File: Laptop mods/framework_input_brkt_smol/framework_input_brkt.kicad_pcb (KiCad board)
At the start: 2 copper layers, 18 x 7.8 mm, 7 parts, among them J1 FPR_LED, J2 input_conn, J3 PWRSW, J4 USB, J6 KBL

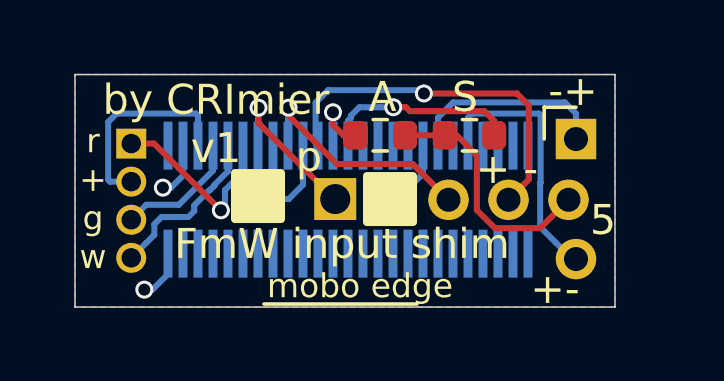
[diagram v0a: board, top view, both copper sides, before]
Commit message: framework_input_brkt_smol: adding resistor to RGW LED, adding Amphenol connector STEP, changing on-board PCB name
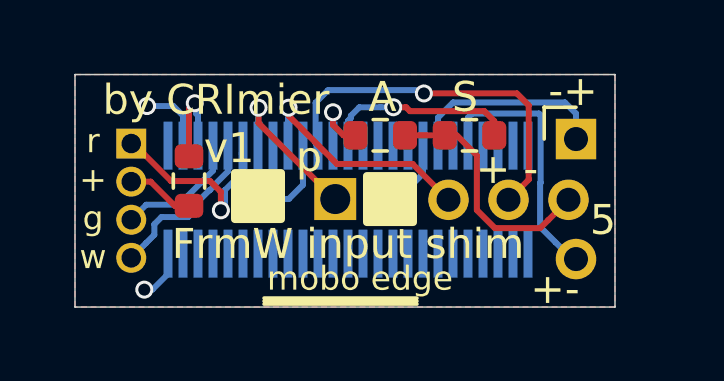
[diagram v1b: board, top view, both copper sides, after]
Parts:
- added R3: 560R, Resistor_SMD:R_0603_1608Metric, F.Cu at (147.8, 99.8)
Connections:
- J1 pad 2: /FPR_LED_COM_5V -> Net-(J1-Pad2)
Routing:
- net /FPR_LED_COM_5V: track 6.86 -> 3.19 mm, vias 0 -> 1
- net Net-(J1-Pad2): track 0.00 -> 2.26 mm
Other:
- board text added: "FrmW input shim"
- board text removed: "FmW input shim"

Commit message: framework_input_brkt_smol: v2, fixed the critical pinout error and rerouted the board; added the caps lock LED connections
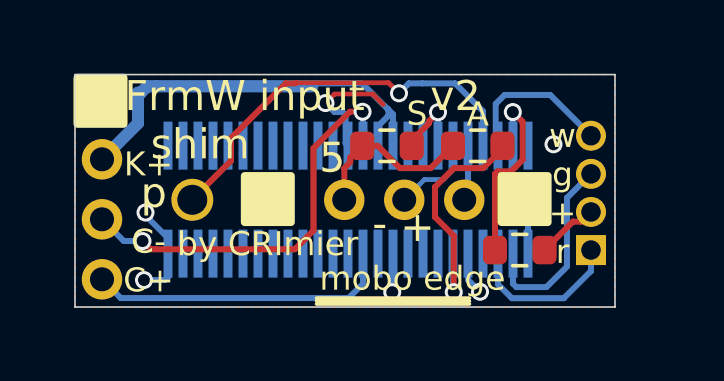
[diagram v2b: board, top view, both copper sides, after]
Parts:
- removed J6: KBL, Connector_PinHeader_2.00mm:PinHeader_1x02_P2.00mm_Vertical
- added J5: KnC, Connector_PinHeader_2.00mm:PinHeader_1x04_P2.00mm_Vertical, F.Cu at (144.9, 97.1)
- J2: value input_conn -> fpc_input_conn
- moved J1 15.7 mm to (161.2, 102.1), turned to 180 degrees
- moved R3 11.3 mm to (158.8, 102.1), turned to 0 degrees
- moved J4 4.53 mm to (159.0, 100.4), turned to 270 degrees
- moved R2 3.27 mm to (157.4, 98.6), turned to 0 degrees
- moved R1 2.77 mm to (154.4, 98.6)
- moved J3 2.23 mm to (150.4, 100.4)
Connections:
- J2 pad 1: Net-(J2-Pad1) -> /KSI0
- J2 pad 10: GND -> /KSO10
- J2 pad 11: /USB_N -> /KSO12
- J2 pad 12: /5VALW -> /KSO14
- J2 pad 13: /5VS -> GND
- J2 pad 14: /TP_BOARD_ID -> /CAPS_N
- J2 pad 15: /TP_SDA -> /KBL_P
- J2 pad 16: /TP_INT -> /KBL_P
- J2 pad 18: GND -> /TP_SDA
- J2 pad 19: /KBL_NP -> /5VS
- J2 pad 2: GND -> /KSI2
- J2 pad 20: Net-(J2-Pad20) -> /USB_N
- J2 pad 21: /KBL_PN -> /USB_P
- J2 pad 22: Net-(J2-Pad22) -> /SWITCH
- J2 pad 23: /CAPS_N -> /FPR_LED_W
- J2 pad 24: /CAPS_P_5V -> /FPR_LED_COM_5V
- J2 pad 26: /KSO15 -> GND
- J2 pad 27: /KSO14 -> /FPR_LED_G
- J2 pad 28: /KSO13 -> /FPR_LED_R
- J2 pad 29: /KSO12 -> /FPR_CTRL
- J2 pad 3: /FPR_LED_COM_5V -> /KSI4
- J2 pad 30: /KSO11 -> GND
- J2 pad 31: /KSO10 -> /5VALW
- J2 pad 32: /KSO9 -> /TP_BOARD_ID
- J2 pad 33: /KSO8 -> /TP_INT
- J2 pad 34: /KSO7 -> GND
- J2 pad 35: /KSO6 -> GND
- J2 pad 36: /KSO5 -> GND
- J2 pad 37: /KSO4 -> /CAPS_P_5V
- J2 pad 38: /KSO3 -> /KSO15
- J2 pad 39: /KSO2 -> /KSO13
- J2 pad 4: /FPR_LED_G -> /KSI6
- J2 pad 40: /KSO1 -> /KSO11
- J2 pad 41: /KSO0 -> /KSO9
- J2 pad 42: /KSI7 -> /KSO7
- J2 pad 43: /KSI6 -> /KSO5
- J2 pad 44: /KSI5 -> /KSO3
- J2 pad 45: /KSI4 -> /KSO1
- J2 pad 46: /KSI3 -> /KSI7
- J2 pad 47: /KSI2 -> /KSI5
- J2 pad 48: /KSI1 -> /KSI3
- J2 pad 49: /KSI0 -> /KSI1
- J2 pad 5: /FPR_LED_W -> /KSO0
- J2 pad 6: /FPR_LED_R -> /KSO2
- J2 pad 7: /SWITCH -> /KSO4
- J2 pad 8: /FPR_CTRL -> /KSO6
- J2 pad 9: /USB_P -> /KSO8
- J3 pad 1: /SWITCH -> GND
- J3 pad 2: GND -> /SWITCH
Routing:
- net /KBL_P: track 0.00 -> 20.1 mm
- net /CAPS_N: track 0.00 -> 13.7 mm, vias 0 -> 2
- net /CAPS_P_5V: track 0.00 -> 10.2 mm
- net /USB_N: track 12.4 -> 2.85 mm, vias 1 -> 0
- net /KBL_PN: track 8.86 -> 0.00 mm
- net /SWITCH: track 5.39 -> 13.6 mm
- net /KBL_NP: track 6.87 -> 0.00 mm
- net /USB_P: track 8.03 -> 1.86 mm, vias 1 -> 0
- net /5VALW: track 2.43 -> 7.94 mm
- net /5VS: track 6.60 -> 2.59 mm
- net /FPR_LED_COM_5V: track 3.19 -> 6.50 mm
- net Net-(J4-Pad4): track 8.19 -> 5.69 mm
- net GND: track 9.78 -> 12.0 mm, vias 2 -> 6
- net /FPR_LED_G: track 4.94 -> 6.55 mm
- net /FPR_LED_R: track 6.99 -> 5.39 mm, vias 1 -> 0
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- added copper zone on B.Cu, net GND
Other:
- rule trace_min: 0.2 -> 0.16
- board text added: "FrmW input v2 shim"
- board text added: "K+ C- C+"
- board text added: "by CRImier"
- board text added: "w g + r"
- board text removed: "+-"
- board text removed: "-+"
- board text removed: "FrmW input shim"
- board text removed: "by CRImier v1"
- board text removed: "r + g w"

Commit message: framework_input_brkt_smol: v2, minor cosmetic and reflow adjustments
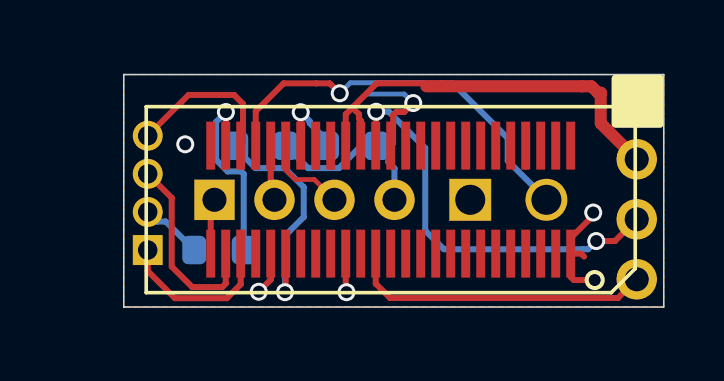
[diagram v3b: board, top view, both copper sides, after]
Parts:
- J1, J3, J4, J5, R1, R2, R3: moved to B.Cu
- J2: moved to F.Cu
- moved J5 17.8 mm to (162.7, 97.1), turned to 180 degrees
- moved J1 14.8 mm to (146.4, 102.1), turned to 0 degrees
- moved J4 10.3 mm to (148.6, 100.4)
- moved R3 10.0 mm to (148.8, 102.1), turned to 180 degrees
- moved R2 7.23 mm to (150.2, 98.6), turned to 180 degrees
- moved J3 6.72 mm to (157.2, 100.4)
- moved J2 1.42 mm to (154.5, 100.4), turned to 180 degrees
- moved R1 1.18 mm to (153.2, 98.6), turned to 0 degrees
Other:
- net class Default removed
- board text added: "FrmW input v3 shim"
- board text removed: "FrmW input v2 shim"
